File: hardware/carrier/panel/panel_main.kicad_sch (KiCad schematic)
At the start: 29 parts, among them J1 GDEY029T94 FPC, J2 CARRIER, J3 FL-A FPC (FL03), J4 FL-B FPC (Orient), J5 FRONTLIGHT, Q5 SI1308EDL

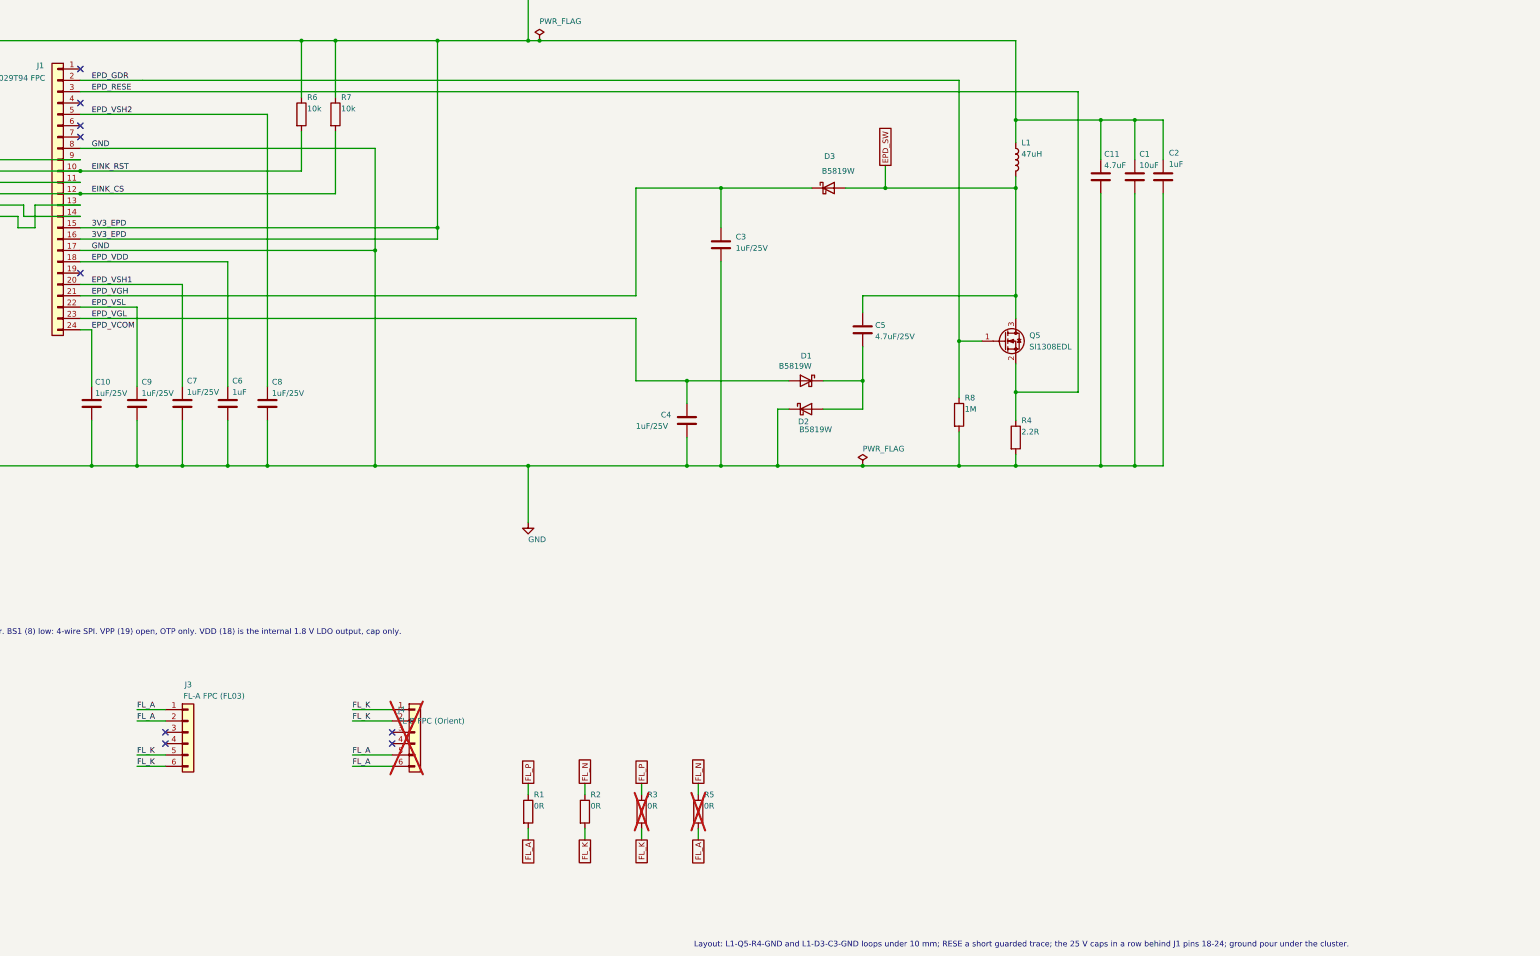
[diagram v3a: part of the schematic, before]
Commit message: Panel: solder-jumper FL polarity, front-light ZIFs at the measured tail offsets
- R1/R2/R3/R5 0R links replaced by JP1/JP2 (SolderJumper 3-pad, 1-2 bridged =
  straight, cut + bridge 2-3 = swapped); no BOM lines, zero height
- J3 (FL03) at J1.x-15.5 in the edge row, J4 (Orient) at J1.x-10.8 one row inboard,
  both on J1's pad-24 side per the Good Display and Orient drawings (the 19 Oct
  placement had FL-A on the pin-1 side)
- jumper block links only; FL_P/FL_N from J5 and the ZIF-to-jumper runs left unrouted
- owner's in-progress hand placement otherwise untouched

Co-Authored-By: Claude Fable 5.1 <noreply@anthropic.com>
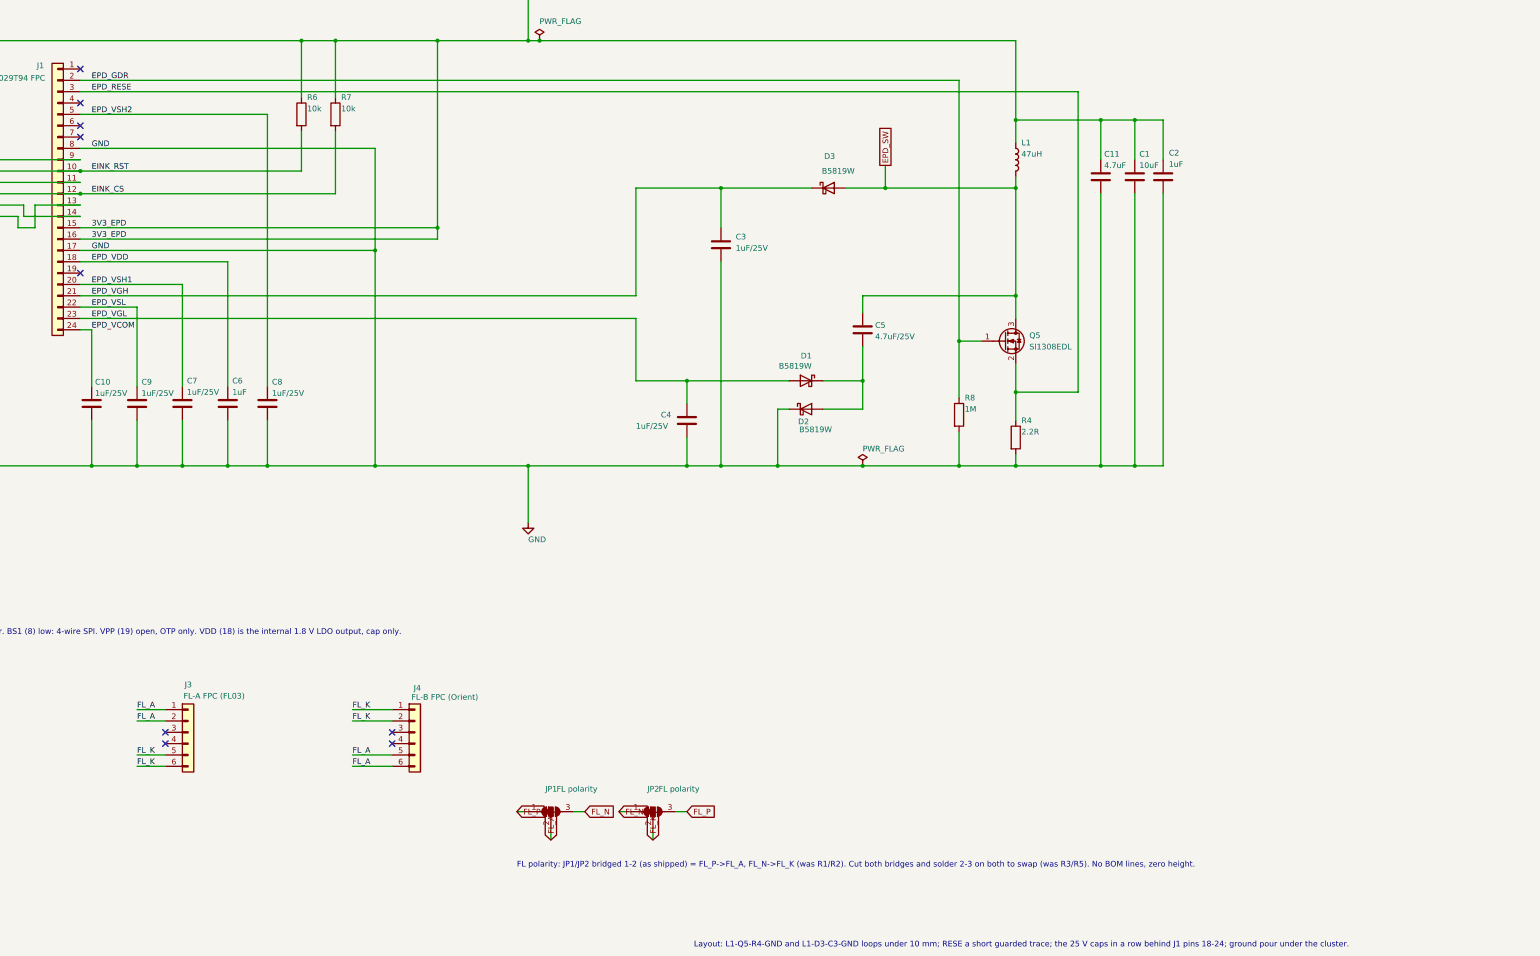
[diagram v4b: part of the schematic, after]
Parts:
- removed R1, R2, R3, R5: 0R, Resistor_SMD:R_0402_1005Metric, symbol Device:R
- added JP1, JP2: FL polarity, Jumper:SolderJumper-3_P1.3mm_Bridged12_RoundedPad1.0x1.5mm, symbol Jumper:SolderJumper_3_Bridged12
- J4: now fitted
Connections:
- net FL_A: now also JP1.2 (C)
- net FL_K: now also JP2.2 (C)
- net FL_N: now also JP1.3 (B), JP2.1 (A)
- net FL_P: now also JP1.1 (A), JP2.3 (B)
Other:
- note added: "FL polarity: JP1/JP2 bridged 1-2 (as shipped) = FL_P->FL_A, FL_N->FL_K (was R1/R2). Cut both bridges and solder 2-3 on both to swap (was R3/R5). No BOM lines, zero height."
